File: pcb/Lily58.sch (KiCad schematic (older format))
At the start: 130 parts, among them J2 4PIN, J3 Conn_01x06_Female, J4 Conn_01x06_Female, P1 i2c_pin, P2 i2c_pin, SW1 SW_PUSH, SW10 SW_PUSH, SW11 SW_PUSH, SW12 SW_PUSH, SW13 SW_PUSH, SW14 SW_PUSH, SW15 SW_PUSH, SW16 SW_PUSH, SW17 SW_PUSH, SW18 SW_PUSH, SW19 SW_PUSH, SW2 SW_PUSH, SW20 SW_PUSH, SW21 SW_PUSH, SW22 SW_PUSH, SW23 SW_PUSH, SW24 SW_PUSH, SW25 SW_PUSH, SW26 SW_PUSH, SW27 SW_PUSH, SW28 SW_PUSH, SW29 SW_PUSH, SW3 SW_PUSH, SW4 SW_PUSH, SW5 SW_PUSH, SW6 SW_PUSH, SW7 SW_PUSH, SW8 SW_PUSH, SW9 SW_PUSH, U1 ProMicro

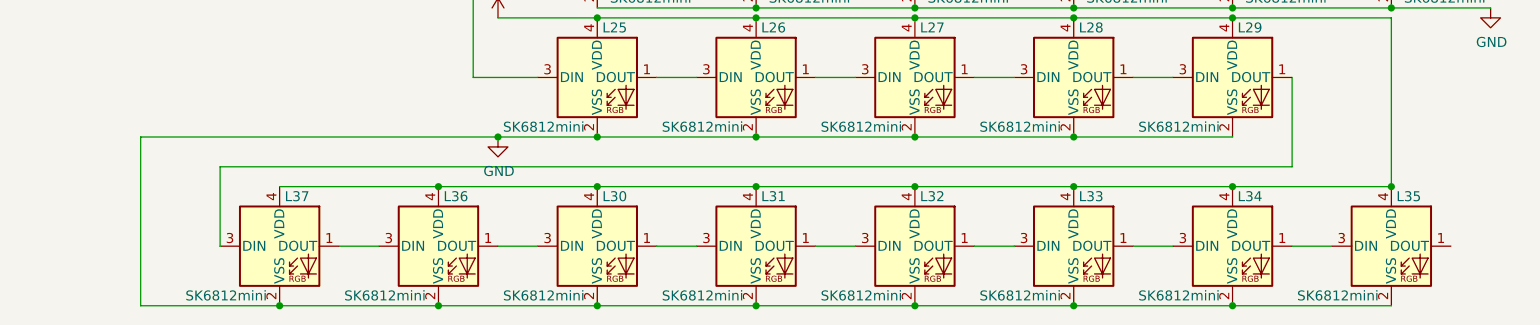
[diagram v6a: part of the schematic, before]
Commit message: update sk6812mini pin assgin
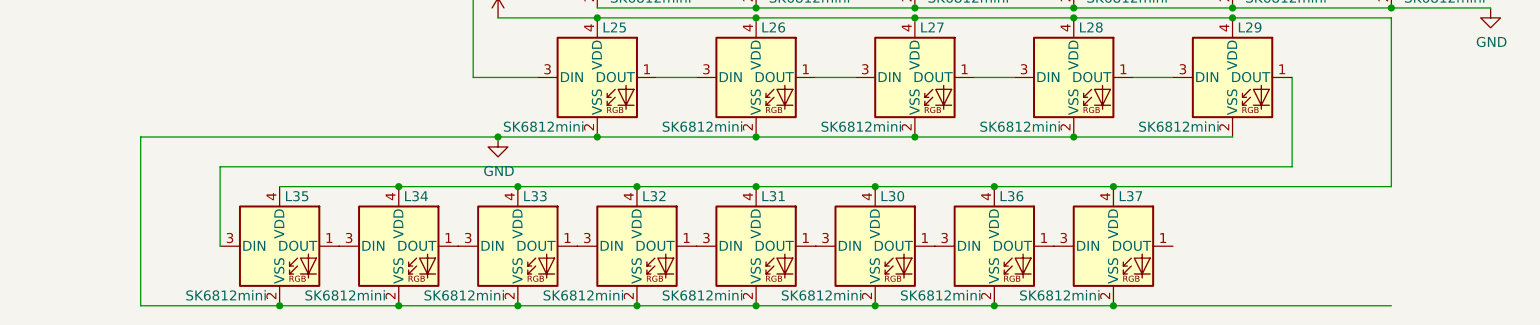
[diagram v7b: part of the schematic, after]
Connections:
- net at L29.1 (DOUT): now also L35.3 (DIN); no longer L37.3 (DIN)
- net at L33.1 (DOUT): now also L32.3 (DIN); no longer L34.3 (DIN)
- net at L33.3 (DIN): now also L34.1 (DOUT); no longer L32.1 (DOUT)
- net at L31.1 (DOUT): now also L30.3 (DIN); no longer L32.3 (DIN)
- net at L31.3 (DIN): now also L32.1 (DOUT); no longer L30.1 (DOUT)
- net at L36.1 (DOUT): now also L37.3 (DIN); no longer L30.3 (DIN)
- net at L35.1 (DOUT): now also L34.3 (DIN)
- net at L36.3 (DIN): now also L30.1 (DOUT); no longer L37.1 (DOUT)
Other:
- moved on the sheet: L30, L32, L33, L34, L35, L36, L37
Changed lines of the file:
@@
 Wire Wire Line
 	2650 7300 2850 7300
-Wire Wire Line
-	7700 10500 7900 10500
-Wire Wire Line
-	6900 10500 7100 10500
 $Comp
 L LED:SK6812MINI L33
 U 1 1 61A4CA14
-P 8200 10500
-F 0 "L33" H 8225 10750 50  0000 L CNN
-F 1 "SK6812mini" H 7725 10250 50  0000 L CNN
-F 2 "Lily58-footprint:SK6812MINI_underglow_rev" H 8250 10200 50  0001 L TNN
-F 3 "https://cdn-shop.adafruit.com/product-files/2686/SK6812MINI_REV.01-1-2.pdf" H 8300 10125 50  0001 L TNN
-	1    8200 10500
+P 5400 10500
+F 0 "L33" H 5425 10750 50  0000 L CNN
+F 1 "SK6812mini" H 4925 10250 50  0000 L CNN
+F 2 "Lily58-footprint:SK6812MINI_underglow_rev" H 5450 10200 50  0001 L TNN
+F 3 "https://cdn-shop.adafruit.com/product-files/2686/SK6812MINI_REV.01-1-2.pdf" H 5500 10125 50  0001 L TNN
+	1    5400 10500
 	1    0    0    -1
 $EndComp
@@
 L LED:SK6812MINI L32
 U 1 1 61A4CA1E
-P 7400 10500
-F 0 "L32" H 7425 10750 50  0000 L CNN
-F 1 "SK6812mini" H 6925 10250 50  0000 L CNN
-F 2 "Lily58-footprint:SK6812MINI_underglow_rev" H 7450 10200 50  0001 L TNN
-F 3 "https://cdn-shop.adafruit.com/product-files/2686/SK6812MINI_REV.01-1-2.pdf" H 7500 10125 50  0001 L TNN
-	1    7400 10500
+P 6000 10500
+F 0 "L32" H 6025 10750 50  0000 L CNN
+F 1 "SK6812mini" H 5525 10250 50  0000 L CNN
+F 2 "Lily58-footprint:SK6812MINI_underglow_rev" H 6050 10200 50  0001 L TNN
+F 3 "https://cdn-shop.adafruit.com/product-files/2686/SK6812MINI_REV.01-1-2.pdf" H 6100 10125 50  0001 L TNN
+	1    6000 10500
 	1    0    0    -1
 $EndComp
-Wire Wire Line
-	6100 10500 6300 10500
 $Comp
 L LED:SK6812MINI L31
@@
 L LED:SK6812MINI L30
 U 1 1 61A4CA33
-P 5800 10500
-F 0 "L30" H 5825 10750 50  0000 L CNN
-F 1 "SK6812mini" H 5325 10250 50  0000 L CNN
-F 2 "Lily58-footprint:SK6812MINI_underglow_rev" H 5850 10200 50  0001 L TNN
-F 3 "https://cdn-shop.adafruit.com/product-files/2686/SK6812MINI_REV.01-1-2.pdf" H 5900 10125 50  0001 L TNN
-	1    5800 10500
+P 7200 10500
+F 0 "L30" H 7225 10750 50  0000 L CNN
+F 1 "SK6812mini" H 6725 10250 50  0000 L CNN
+F 2 "Lily58-footprint:SK6812MINI_underglow_rev" H 7250 10200 50  0001 L TNN
+F 3 "https://cdn-shop.adafruit.com/product-files/2686/SK6812MINI_REV.01-1-2.pdf" H 7300 10125 50  0001 L TNN
+	1    7200 10500
 	1    0    0    -1
 $EndComp
@@
 L LED:SK6812MINI L34
 U 1 1 61A4CA3D
-P 9000 10500
-F 0 "L34" H 9025 10750 50  0000 L CNN
-F 1 "SK6812mini" H 8525 10250 50  0000 L CNN
-F 2 "Lily58-footprint:SK6812MINI_underglow_rev" H 9050 10200 50  0001 L TNN
-F 3 "https://cdn-shop.adafruit.com/product-files/2686/SK6812MINI_REV.01-1-2.pdf" H 9100 10125 50  0001 L TNN
-	1    9000 10500
+P 4800 10500
+F 0 "L34" H 4825 10750 50  0000 L CNN
+F 1 "SK6812mini" H 4325 10250 50  0000 L CNN
+F 2 "Lily58-footprint:SK6812MINI_underglow_rev" H 4850 10200 50  0001 L TNN
+F 3 "https://cdn-shop.adafruit.com/product-files/2686/SK6812MINI_REV.01-1-2.pdf" H 4900 10125 50  0001 L TNN
+	1    4800 10500
+	1    0    0    -1
+$EndComp
+$Comp
+L LED:SK6812MINI L35
+U 1 1 61A7E919
+P 4200 10500
+F 0 "L35" H 4225 10750 50  0000 L CNN
+F 1 "SK6812mini" H 3725 10250 50  0000 L CNN
+F 2 "Lily58-footprint:SK6812MINI_underglow_rev" H 4250 10200 50  0001 L TNN
+F 3 "https://cdn-shop.adafruit.com/product-files/2686/SK6812MINI_REV.01-1-2.pdf" H 4300 10125 50  0001 L TNN
+	1    4200 10500
 	1    0    0    -1
 $EndComp
 Wire Wire Line
-	8500 10500 8700 10500
-$Comp
-L LED:SK6812MINI L35
-U 1 1 61A7E919
-P 9800 10500
-F 0 "L35" H 9825 10750 50  0000 L CNN
-F 1 "SK6812mini" H 9325 10250 50  0000 L CNN
-F 2 "Lily58-footprint:SK6812MINI_underglow_rev" H 9850 10200 50  0001 L TNN
-F 3 "https://cdn-shop.adafruit.com/product-files/2686/SK6812MINI_REV.01-1-2.pdf" H 9900 10125 50  0001 L TNN
-	1    9800 10500
-	1    0    0    -1
-$EndComp
-Wire Wire Line
-	9300 10500 9500 10500
-Wire Wire Line
-	5800 10200 6600 10200
-Connection ~ 6600 10200
-Wire Wire Line
-	6600 10200 7400 10200
-Connection ~ 7400 10200
-Wire Wire Line
-	7400 10200 8200 10200
-Connection ~ 8200 10200
-Wire Wire Line
-	8200 10200 9000 10200
-Connection ~ 9000 10200
-Wire Wire Line
-	9000 10200 9800 10200
-Wire Wire Line
 	9000 9350 9800 9350
 Connection ~ 9000 9350
-Connection ~ 9800 10200
-Wire Wire Line
-	9800 10800 9000 10800
-Connection ~ 5800 10800
-Connection ~ 6600 10800
-Wire Wire Line
-	6600 10800 5800 10800
-Connection ~ 7400 10800
-Wire Wire Line
-	7400 10800 6600 10800
-Connection ~ 8200 10800
-Wire Wire Line
-	8200 10800 7400 10800
-Connection ~ 9000 10800
-Wire Wire Line
-	9000 10800 8200 10800
 Wire Wire Line
 	5300 9950 5800 9950
@@
 L LED:SK6812MINI L36
 U 1 1 61AA0F7C
-P 5000 10500
-F 0 "L36" H 5025 10750 50  0000 L CNN
-F 1 "SK6812mini" H 4525 10250 50  0000 L CNN
-F 2 "Lily58-footprint:SK6812MINI_underglow_rev" H 5050 10200 50  0001 L TNN
-F 3 "https://cdn-shop.adafruit.com/product-files/2686/SK6812MINI_REV.01-1-2.pdf" H 5100 10125 50  0001 L TNN
-	1    5000 10500
+P 7800 10500
+F 0 "L36" H 7825 10750 50  0000 L CNN
+F 1 "SK6812mini" H 7325 10250 50  0000 L CNN
+F 2 "Lily58-footprint:SK6812MINI_underglow_rev" H 7850 10200 50  0001 L TNN
+F 3 "https://cdn-shop.adafruit.com/product-files/2686/SK6812MINI_REV.01-1-2.pdf" H 7900 10125 50  0001 L TNN
+	1    7800 10500
 	1    0    0    -1
 $EndComp
-Wire Wire Line
-	5300 10500 5500 10500
-Wire Wire Line
-	5000 10800 5800 10800
-Wire Wire Line
-	5000 10200 5800 10200
-Connection ~ 5800 10200
-Connection ~ 5000 10800
 Connection ~ 5300 9950
 Wire Wire Line
@@
 L LED:SK6812MINI L37
 U 1 1 61A982D1
-P 4200 10500
-F 0 "L37" H 4225 10750 50  0000 L CNN
-F 1 "SK6812mini" H 3725 10250 50  0000 L CNN
-F 2 "Lily58-footprint:SK6812MINI_underglow_rev" H 4250 10200 50  0001 L TNN
-F 3 "https://cdn-shop.adafruit.com/product-files/2686/SK6812MINI_REV.01-1-2.pdf" H 4300 10125 50  0001 L TNN
-	1    4200 10500
+P 8400 10500
+F 0 "L37" H 8425 10750 50  0000 L CNN
+F 1 "SK6812mini" H 7925 10250 50  0000 L CNN
+F 2 "Lily58-footprint:SK6812MINI_underglow_rev" H 8450 10200 50  0001 L TNN
+F 3 "https://cdn-shop.adafruit.com/product-files/2686/SK6812MINI_REV.01-1-2.pdf" H 8500 10125 50  0001 L TNN
+	1    8400 10500
 	1    0    0    -1
 $EndComp
-Wire Wire Line
-	4200 10800 5000 10800
-Wire Wire Line
-	4200 10800 3500 10800
 Wire Wire Line
 	3500 10800 3500 9950
 Wire Wire Line
 	3500 9950 5300 9950
-Connection ~ 4200 10800
 Wire Wire Line
 	3900 10100 3900 10500
@@
 	3900 10100 9300 10100
 Wire Wire Line
-	4500 10500 4700 10500
+	4200 10200 4800 10200
 Wire Wire Line
-	4200 10200 5000 10200
-Connection ~ 5000 10200
+	3500 10800 4200 10800
+Connection ~ 4200 10800
+Wire Wire Line
+	4200 10800 4800 10800
+Connection ~ 4800 10200
+Wire Wire Line
+	4800 10200 5400 10200
+Connection ~ 4800 10800
+Wire Wire Line
+	4800 10800 5400 10800
+Connection ~ 5400 10200
+Wire Wire Line
+	5400 10200 6000 10200
+Connection ~ 5400 10800
+Wire Wire Line
+	5400 10800 6000 10800
+Connection ~ 6000 10200
+Wire Wire Line
+	6000 10200 6600 10200
+Connection ~ 6000 10800
+Wire Wire Line
+	6000 10800 6600 10800
+Connection ~ 6600 10200
+Wire Wire Line
+	6600 10200 7200 10200
+Connection ~ 6600 10800
+Wire Wire Line
+	6600 10800 7200 10800
+Connection ~ 7200 10200
+Wire Wire Line
+	7200 10200 7800 10200
+Connection ~ 7200 10800
+Wire Wire Line
+	7200 10800 7800 10800
+Connection ~ 7800 10200
+Wire Wire Line
+	7800 10200 8400 10200
+Connection ~ 7800 10800
+Wire Wire Line
+	7800 10800 8400 10800
+Connection ~ 8400 10200
+Wire Wire Line
+	8400 10200 9800 10200
+Connection ~ 8400 10800
+Wire Wire Line
+	8400 10800 9800 10800
 $EndSCHEMATC

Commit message: change pcb - delete underglow - change pins - change holes for sk6812mini-e
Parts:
- removed L30, L31, L32, L33, L34, L35, L36, L37: SK6812mini, Lily58-footprint:SK6812MINI_underglow_rev, symbol LED:SK6812MINI
- added JP17, JP18, JP19, JP20: Jumper_NO_Small, Lily58-footprint:Jumper, symbol Device:Jumper_NO_Small
- added TH8, TH9: HOLE, Lily58-footprint:HOLE_M2, symbol Lily58-rescue:HOLE-Lily58-cache
- J4: footprint Lily58-footprint:OLED_4Pin -> Lily58-footprint:OLED_6Pin; symbol Lily58-rescue:CONN_01X04-Lily58-cache -> Lily58-rescue:CONN_01X06-Lily58-cache
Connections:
- net A2: now also U1.18 (A1(PF6)), JP17.2; no longer JP11.2, U1.19 (A2(PF5))
- net A3: now also JP10.2, JP19.2; no longer JP12.2, JP13.2
- net GND: now also JP11.2, JP16.2
- net VCC: now also JP9.2, JP20.2
- net col0: now also JP12.2, U1.19 (A2(PF5)); no longer JP10.2, U1.18 (A1(PF6))
- net row4: now also JP13.2, JP18.2; no longer JP16.2, JP9.2
- new net: J4.5 (P5), JP17.1, JP19.1
- new net: J4.6 (P6), JP18.1, JP20.1
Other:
- moved on the sheet: JP13, JP14, JP15, JP16
